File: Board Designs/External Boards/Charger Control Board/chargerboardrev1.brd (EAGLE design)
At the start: 49.5 x 41.6 mm, 17 parts, among them X1 CONNECTOR-6NANO-FIT_VERTICAL-6, X3 CONNECTOR-2, X4 CONNECTOR-2

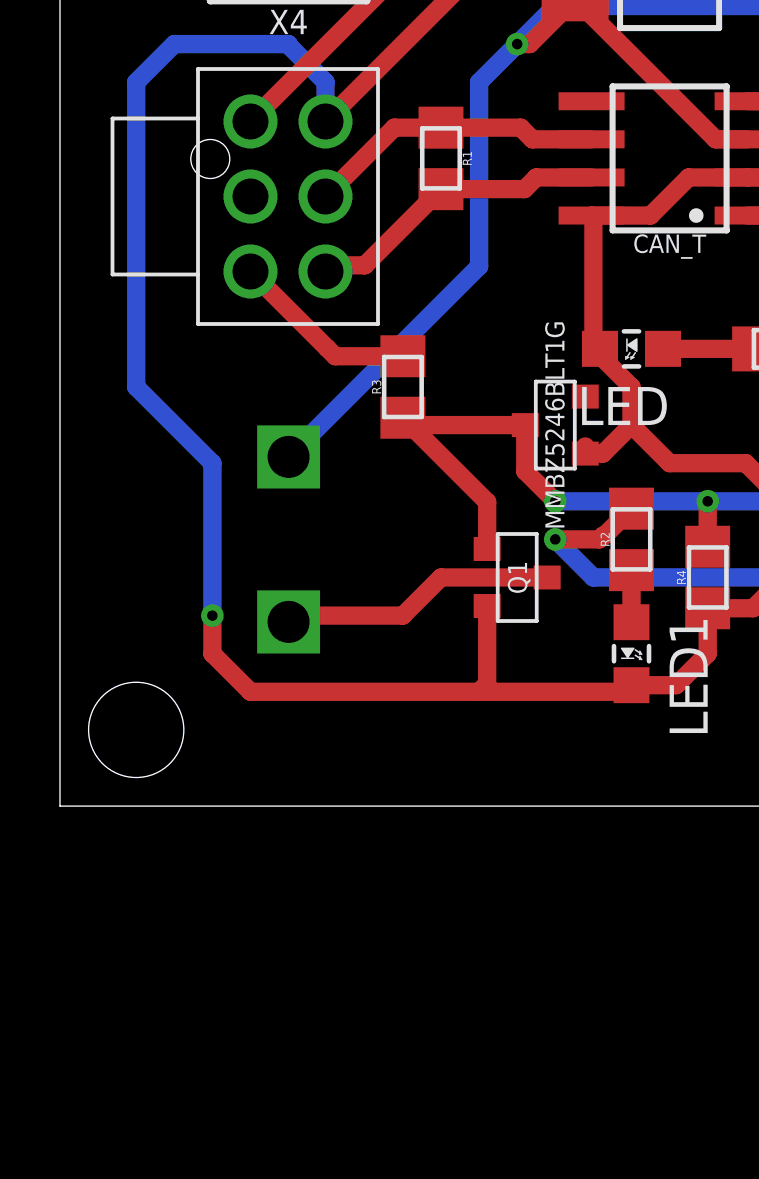
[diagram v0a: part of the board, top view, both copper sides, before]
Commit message: added jumper and added capacitor to 5v reg
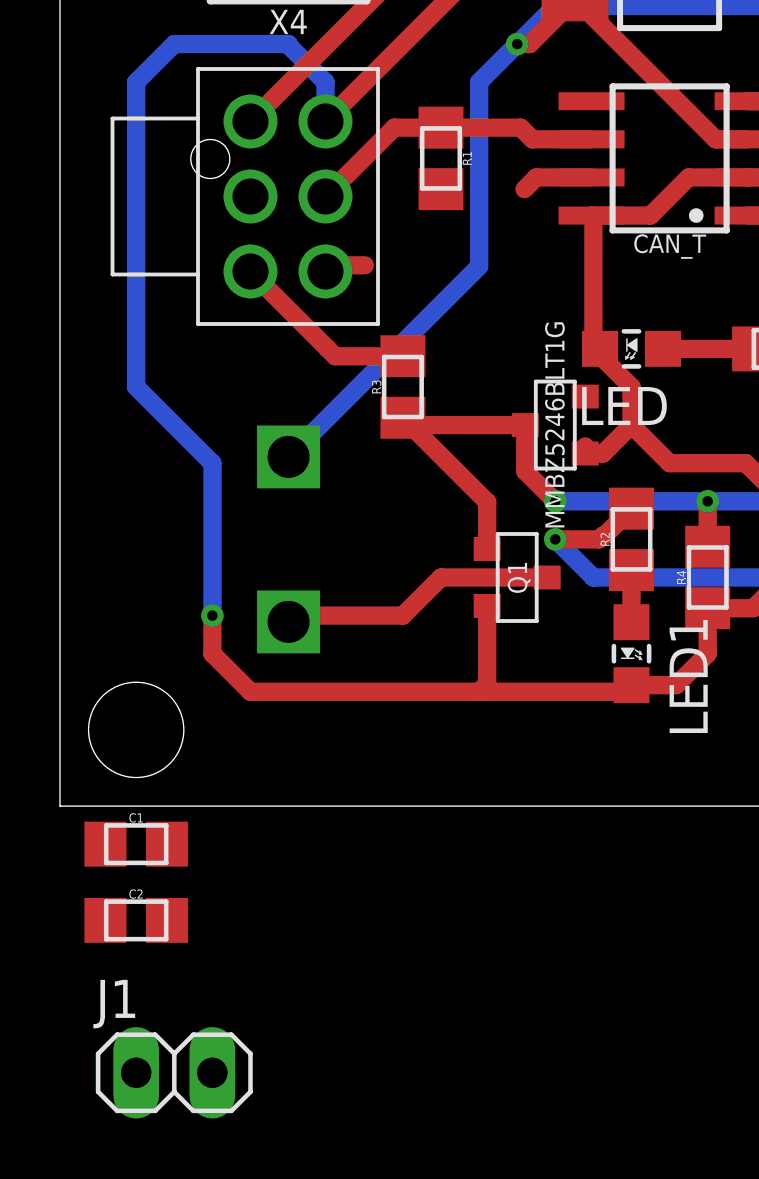
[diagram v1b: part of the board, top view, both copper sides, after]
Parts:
- added C1, C2: 0.22uF, HyTechDevices:0805
- added J1: JUMPER.1, HyTechDevices:1X02
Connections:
- new net N$5: J1.1, R1.2
- net 12V: now also C1.1
- net 5V: now also C2.1
- net CANH: now also J1.2; no longer R1.2
- net GND: now also C1.2, C2.2
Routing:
- net CANH: track 10.6 -> 4.20 mm
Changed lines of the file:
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@@
 <element name="U$3" library="HyTechDevices" package="SOP04" value="CPC1002N" x="129.54" y="35.56" rot="R90"/>
 <element name="R6" library="HyTechDevices" package="0805" value="330" x="135.89" y="34.29" rot="R180"/>
+<element name="C1" library="HyTechDevices" package="0805" value="0.22uF" x="114.3" y="-2.54"/>
+<element name="C2" library="HyTechDevices" package="0805" value="0.22uF" x="114.3" y="-5.08"/>
+<element name="J1" library="HyTechDevices" package="1X02" value="JUMPER.1" x="115.57" y="-10.16"/>
 </elements>
 <signals>
@@
 <wire x1="128.93" y1="25.64" x2="127.42" y2="24.13" width="0.6096" layer="1"/>
 <wire x1="127.42" y1="24.13" x2="127" y2="24.13" width="0.6096" layer="1"/>
+<contactref element="C2" pad="1"/>
+<wire x1="113.275" y1="-5.08" x2="119.38" y2="10.37" width="0" layer="19" extent="1-1"/>
 </signal>
 <signal name="GND">
@@
 <wire x1="130.81" y1="12.7" x2="129.76" y2="13.75" width="0.6096" layer="1"/>
 <wire x1="129.76" y1="13.75" x2="129.76" y2="13.97" width="0.6096" layer="1"/>
+<contactref element="C1" pad="2"/>
+<contactref element="C2" pad="2"/>
+<wire x1="115.325" y1="-2.54" x2="118.11" y2="2.54" width="0" layer="19" extent="1-1"/>
+<wire x1="115.325" y1="-5.08" x2="115.325" y2="-2.54" width="0" layer="19" extent="1-1"/>
 </signal>
 <signal name="CANRX">
@@
 <signal name="CANH">
 <contactref element="CAN_T" pad="7"/>
-<contactref element="R1" pad="2"/>
-<wire x1="124.46" y1="19.295" x2="127.245" y2="19.295" width="0.6096" layer="1"/>
 <wire x1="127.245" y1="19.295" x2="127.635" y2="19.685" width="0.6096" layer="1"/>
 <wire x1="127.635" y1="19.685" x2="129.48" y2="19.685" width="0.6096" layer="1"/>
@@
 <wire x1="120.815" y1="16.755" x2="120.61" y2="16.755" width="0.6096" layer="1"/>
 <wire x1="120.61" y1="16.755" x2="121.92" y2="16.755" width="0.6096" layer="1"/>
-<wire x1="121.92" y1="16.755" x2="124.46" y2="19.295" width="0.6096" layer="1"/>
 <wire x1="120.815" y1="16.755" x2="120.61" y2="16.55" width="0.6096" layer="1"/>
+<contactref element="J1" pad="2"/>
+<wire x1="121.92" y1="16.755" x2="127.245" y2="19.295" width="0" layer="19" extent="1-1"/>
+<wire x1="116.84" y1="-10.16" x2="120.61" y2="16.55" width="0" layer="19" extent="1-1"/>
 </signal>
 <signal name="CANL">
@@
 <wire x1="118.11" y1="21.55" x2="126.8" y2="30.24" width="0.6096" layer="1"/>
 <wire x1="126.8" y1="30.24" x2="128.93" y2="30.24" width="0.6096" layer="1"/>
+<contactref element="C1" pad="1"/>
+<wire x1="113.275" y1="-2.54" x2="118.11" y2="21.55" width="0" layer="19" extent="1-1"/>
 </signal>
 <signal name="N$1">
@@
 <wire x1="129.9172" y1="7.7522" x2="130.81" y2="8.645" width="0.6096" layer="1"/>
 </signal>
+<signal name="N$5">
+<contactref element="R1" pad="2"/>
+<contactref element="J1" pad="1"/>
+<wire x1="114.3" y1="-10.16" x2="124.46" y2="19.295" width="0" layer="19" extent="1-1"/>
+</signal>
 </signals>

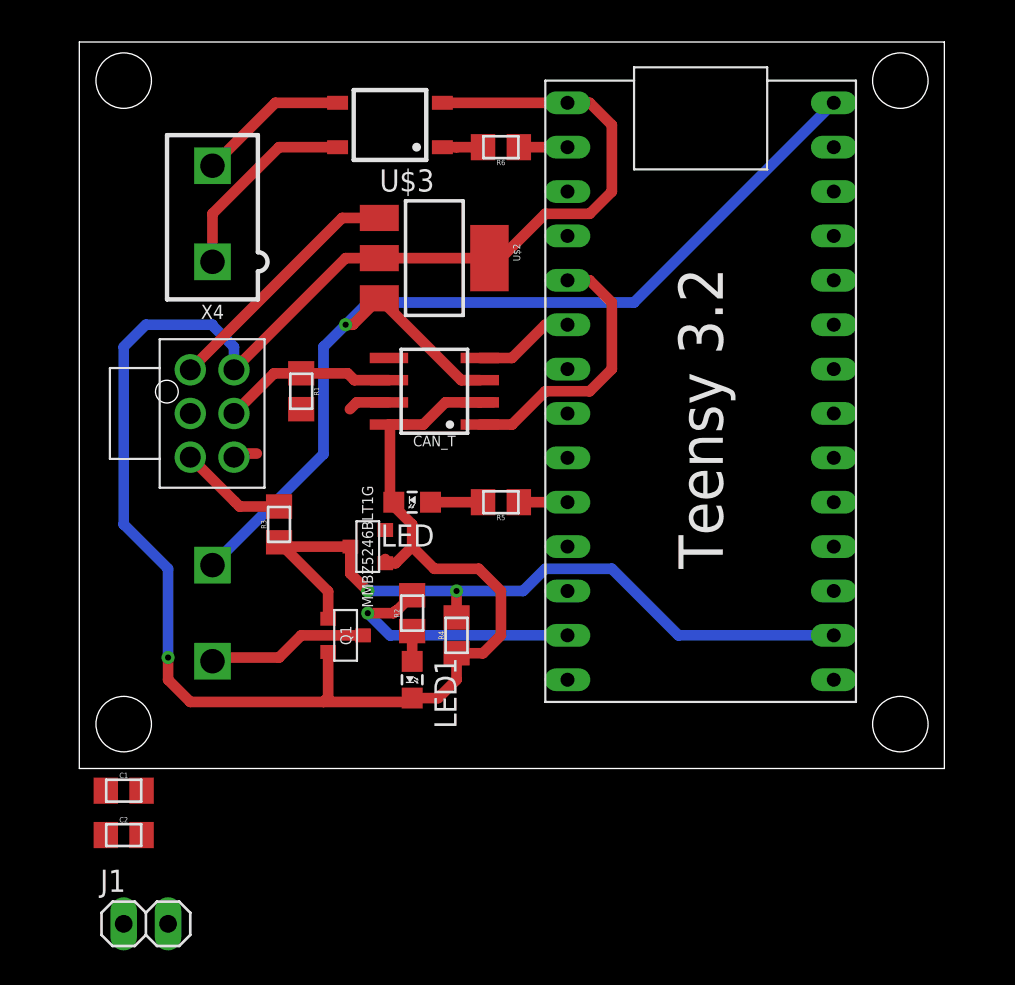
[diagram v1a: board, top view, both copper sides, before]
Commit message: Charger Control Board with suggested modifications
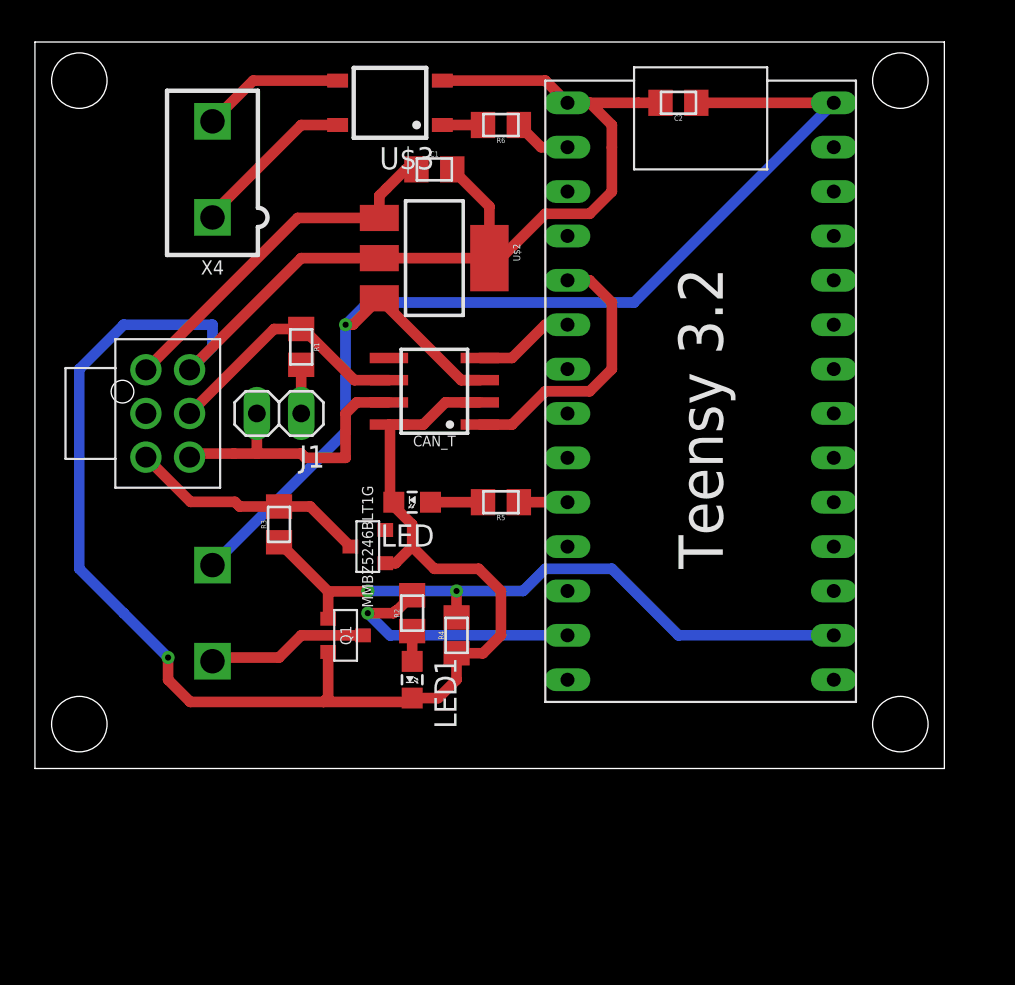
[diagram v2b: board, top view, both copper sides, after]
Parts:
- moved C2 52.6 mm to (146.1, 36.8), turned to 180 degrees
- moved C1 39.8 mm to (132.1, 33.0)
- moved J1 30.2 mm to (123.2, 19.1), turned to 180 degrees
- moved X1 2.54 mm to (115.6, 19.1)
- moved X4 2.54 mm to (119.4, 33.0)
- moved R1 2.54 mm to (124.5, 22.9)
- moved R6 1.27 mm to (135.9, 35.6)
- moved U$3 1.27 mm to (129.5, 36.8)
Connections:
- net CHARGE_ENABLE: now also MMBZ5246BLT1G.3
- net SIGNAL_SAFE: no longer MMBZ5246BLT1G.3
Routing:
- net GND: track 118.6 -> 133.5 mm
- net CANH: track 4.20 -> 16.7 mm
- net CHARGE_ENABLE: track 6.25 -> 13.8 mm
- net 5V: track 60.7 -> 68.2 mm
- net 12V: track 14.4 -> 21.0 mm
- net SIGNAL_SAFE: track 43.0 -> 38.1 mm
- net CANL: track 10.2 -> 14.6 mm
- net N$5: track 0.00 -> 2.79 mm
- net N$8: track 11.5 -> 9.47 mm
- net N$7: track 8.65 -> 8.13 mm
- net CHRG_C: track 2.78 -> 3.31 mm
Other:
- board size 49.5 x 41.6 mm -> 52.1 x 41.6 mm

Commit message: Charger control board with modifications to control external relay board
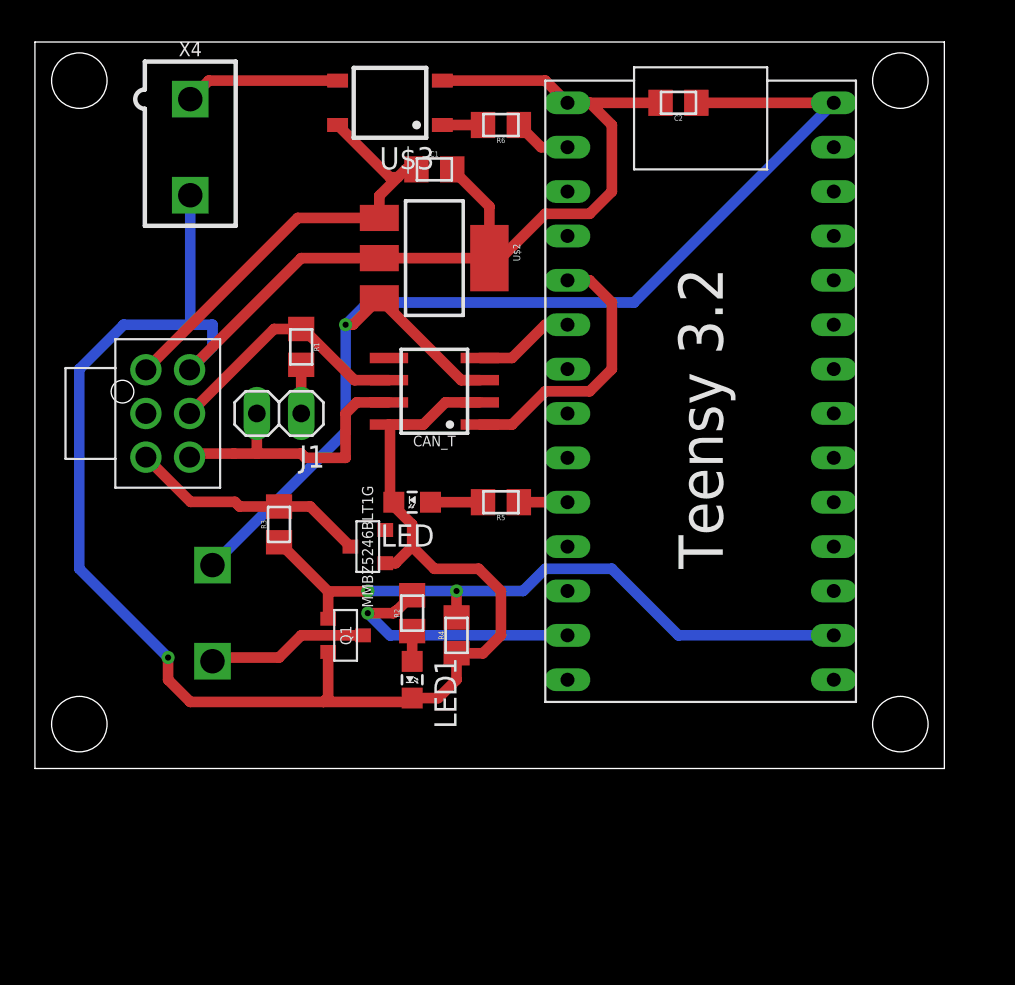
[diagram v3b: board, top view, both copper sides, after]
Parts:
- moved X4 1.80 mm to (118.1, 34.3), turned to 180 degrees
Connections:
- removed net N$8: U$3.4, X4.1
- net 12V: now also U$3.4
- net GND: now also X4.2
- net N$7: now also X4.1; no longer X4.2
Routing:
- net N$8: track 9.47 -> 0.00 mm
- net GND: track 133.5 -> 140.9 mm
- net 12V: track 21.0 -> 25.7 mm
- net N$7: track 8.13 -> 8.87 mm
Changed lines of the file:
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@@
 <element name="LED" library="HyTechDevices" package="LED-805" value="" x="130.81" y="13.97" rot="R90"/>
 <element name="R5" library="HyTechDevices" package="0805" value="1.2k" x="135.89" y="13.97" rot="R180"/>
-<element name="X4" library="HyTechDevices" package="MINIFIT_5566-2" value="CONNECTOR-2" x="119.38" y="33.02">
-<attribute name="MF" value="" x="119.38" y="33.02" size="1.778" layer="27" display="off"/>
-<attribute name="MPN" value="" x="119.38" y="33.02" size="1.778" layer="27" display="off"/>
-<attribute name="OC_FARNELL" value="1822072" x="119.38" y="33.02" size="1.778" layer="27" display="off"/>
-<attribute name="OC_NEWARK" value="unknown" x="119.38" y="33.02" size="1.778" layer="27" display="off"/>
+<element name="X4" library="HyTechDevices" package="MINIFIT_5566-2" value="CONNECTOR-2" x="118.11" y="34.29" rot="R180">
+<attribute name="MF" value="" x="118.11" y="34.29" size="1.778" layer="27" rot="R180" display="off"/>
+<attribute name="MPN" value="" x="118.11" y="34.29" size="1.778" layer="27" rot="R180" display="off"/>
+<attribute name="OC_FARNELL" value="1822072" x="118.11" y="34.29" size="1.778" layer="27" rot="R180" display="off"/>
+<attribute name="OC_NEWARK" value="unknown" x="118.11" y="34.29" size="1.778" layer="27" rot="R180" display="off"/>
 </element>
 <element name="U$3" library="HyTechDevices" package="SOP04" value="CPC1002N" x="129.54" y="36.83" rot="R90"/>
@@
 <wire x1="139.7" y1="36.83" x2="140.97" y2="36.83" width="0.6096" layer="1"/>
 <wire x1="140.97" y1="36.83" x2="142.24" y2="35.56" width="0.6096" layer="1"/>
-<wire x1="142.24" y1="35.56" x2="142.24" y2="34.29" width="0.6096" layer="1"/>
 <wire x1="140.97" y1="30.48" x2="138.43" y2="30.48" width="0.6096" layer="1"/>
 <wire x1="138.43" y1="30.48" x2="135.89" y2="27.94" width="0.6096" layer="1"/>
@@
 <wire x1="126" y1="5.4" x2="126" y2="2.81" width="0.6096" layer="1"/>
 <wire x1="126" y1="2.81" x2="125.73" y2="2.54" width="0.6096" layer="1"/>
-<wire x1="111.76" y1="10.16" x2="114.3" y2="7.62" width="0.6096" layer="16"/>
-<wire x1="114.3" y1="7.62" x2="116.84" y2="5.08" width="0.6096" layer="16"/>
-<wire x1="114.3" y1="24.13" x2="119.38" y2="24.13" width="0.6096" layer="16"/>
+<wire x1="111.76" y1="10.16" x2="116.84" y2="5.08" width="0.6096" layer="16"/>
+<wire x1="114.3" y1="24.13" x2="118.11" y2="24.13" width="0.6096" layer="16"/>
+<wire x1="118.11" y1="24.13" x2="119.38" y2="24.13" width="0.6096" layer="16"/>
 <wire x1="118.11" y1="2.54" x2="116.84" y2="3.81" width="0.6096" layer="1"/>
 <wire x1="116.84" y1="3.81" x2="116.84" y2="5.08" width="0.6096" layer="1"/>
@@
 <wire x1="133.105" y1="33.02" x2="135.23" y2="30.895" width="0.6096" layer="1"/>
 <wire x1="135.23" y1="30.895" x2="135.23" y2="27.94" width="0.6096" layer="1"/>
-<wire x1="140.97" y1="36.83" x2="143.755" y2="36.83" width="0.6096" layer="1"/>
-<wire x1="142.24" y1="34.29" x2="142.24" y2="31.75" width="0.6096" layer="1"/>
-<wire x1="143.755" y1="36.83" x2="145.025" y2="36.83" width="0.6096" layer="1"/>
+<wire x1="140.97" y1="36.83" x2="145.025" y2="36.83" width="0.6096" layer="1"/>
+<wire x1="142.24" y1="35.56" x2="142.24" y2="31.75" width="0.6096" layer="1"/>
+<contactref element="X4" pad="2"/>
+<wire x1="118.11" y1="31.54" x2="118.11" y2="24.13" width="0.6096" layer="16"/>
 </signal>
 <signal name="CANRX">
@@
 <wire x1="124.26" y1="30.24" x2="128.93" y2="30.24" width="0.6096" layer="1"/>
 <contactref element="C1" pad="1"/>
-<wire x1="128.93" y1="31.51" x2="129.355" y2="31.935" width="0.6096" layer="1"/>
 <wire x1="128.93" y1="30.24" x2="128.93" y2="31.51" width="0.6096" layer="1"/>
-<wire x1="129.355" y1="31.935" x2="130.44" y2="33.02" width="0.6096" layer="1"/>
+<wire x1="128.93" y1="31.51" x2="129.99" y2="32.57" width="0.6096" layer="1"/>
+<wire x1="129.99" y1="32.57" x2="130.44" y2="33.02" width="0.6096" layer="1"/>
 <wire x1="130.44" y1="33.02" x2="131.055" y2="33.02" width="0.6096" layer="1"/>
+<contactref element="U$3" pad="4"/>
+<wire x1="126.54" y1="35.56" x2="129.53" y2="32.57" width="0.6096" layer="1"/>
+<wire x1="129.53" y1="32.57" x2="129.99" y2="32.57" width="0.6096" layer="1"/>
 </signal>
 <signal name="N$1">
@@
 <contactref element="LED" pad="A"/>
 <wire x1="134.865" y1="13.97" x2="131.86" y2="13.97" width="0.6096" layer="1"/>
-</signal>
-<signal name="N$7">
-<contactref element="U$3" pad="3"/>
-<contactref element="X4" pad="2"/>
-<wire x1="121.71" y1="38.1" x2="119.38" y2="35.77" width="0.6096" layer="1"/>
-<wire x1="126.54" y1="38.1" x2="121.71" y2="38.1" width="0.6096" layer="1"/>
-</signal>
-<signal name="N$8">
-<contactref element="X4" pad="1"/>
-<contactref element="U$3" pad="4"/>
-<wire x1="126.54" y1="35.56" x2="124.46" y2="35.56" width="0.6096" layer="1"/>
-<wire x1="124.46" y1="35.56" x2="119.38" y2="30.48" width="0.6096" layer="1"/>
-<wire x1="119.38" y1="30.48" x2="119.38" y2="30.27" width="0.6096" layer="1"/>
 </signal>
 <signal name="N$10">
@@
 <wire x1="124.46" y1="21.835" x2="124.46" y2="19.05" width="0.6096" layer="1"/>
 </signal>
+<signal name="N$7">
+<contactref element="U$3" pad="3"/>
+<contactref element="X4" pad="1"/>
+<wire x1="119.17" y1="38.1" x2="126.54" y2="38.1" width="0.6096" layer="1"/>
+<wire x1="118.11" y1="37.04" x2="119.17" y2="38.1" width="0.6096" layer="1"/>
+</signal>
 </signals>
 <mfgpreviewcolors>
@@
 <mfgpreviewcolor name="substratecolor" color="0xFF786E46"/>
 </mfgpreviewcolors>
+<errors>
+</errors>
 </board>
 </drawing>

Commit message: Made final changes to Charger Boards. Added a relay to Library
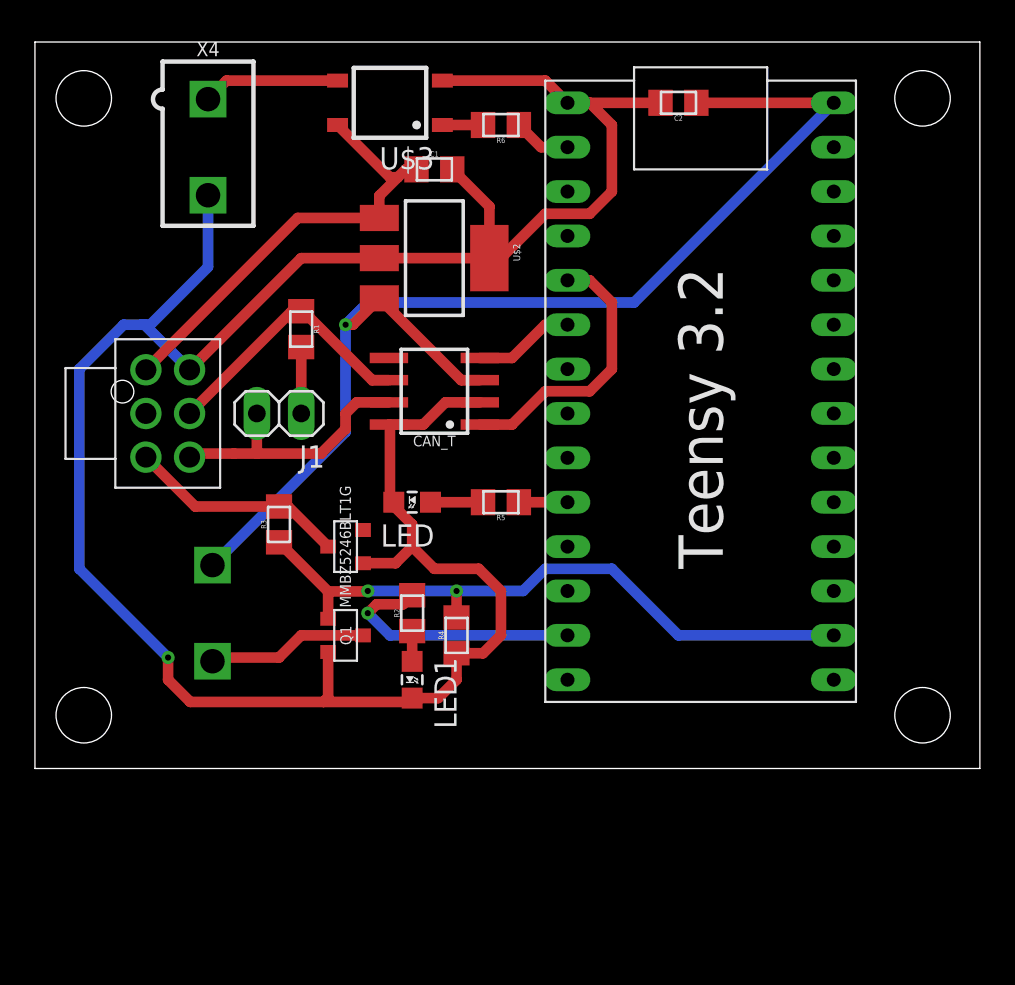
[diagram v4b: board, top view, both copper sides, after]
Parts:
- moved MMBZ5246BLT1G 1.27 mm to (127.0, 11.4)
- moved X4 1.02 mm to (119.1, 34.3)
- moved R1 1.02 mm to (124.5, 23.9)
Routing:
- net CHARGE_ENABLE: track 13.8 -> 12.6 mm
- net CANH: track 16.7 -> 15.5 mm
- net N$7: track 8.87 -> 7.85 mm
- net N$5: track 2.79 -> 3.80 mm
- net CANL: track 14.6 -> 15.5 mm
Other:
- board size 52.1 x 41.6 mm -> 54.1 x 41.6 mm
- board text added: "Designed by: Dean Plaskon"
- board text added: "HyTech Racing 2019 Charger Board Rev1"
